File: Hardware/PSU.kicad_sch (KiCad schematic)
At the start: 0 parts

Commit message: included psu on pcb
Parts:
- added C? (x7): 10u, symbol Device:C_Polarized_Small
- added C?: 10n, symbol Device:C_Small
- added C?: 100n, symbol Device:C_Small
- added F?: BELFUSE 430021 2,5A, symbol Device:Fuse_Small
- added L?: BLM21PG 221, symbol Device:L_Ferrite_Small
- added Q?: FDN 337N, symbol Device:Q_NMOS_GSD
- added U? (x3): AP1117-33, Package_TO_SOT_SMD:SOT-223-3_TabPin2, symbol Regulator_Linear:AP1117-33
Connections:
- new net: C?.1, C?.1, C?.1, C?.1, F?.2, L?.1, U?.3 (VI), U?.3 (VI), U?.3 (VI)
- new net: F?.1, Q?.2 (S)
- new net 3V3_0: C?.1, U?.2 (VO)
- new net 3V3_1: C?.1, U?.2 (VO)
- new net 3V3_2: C?.1, U?.2 (VO)
- new net 5V: Q?.3 (D)
- new net GND: C?.2, C?.2, C?.2, C?.2, C?.2, C?.2, C?.2, C?.2, C?.2, Q?.1 (G), U?.1 (GND), U?.1 (GND), U?.1 (GND)
- new net PWR: C?.1, C?.1, L?.2
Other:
- note added: "TODO: 1. LiPo Batterie integration 2. Step Up"

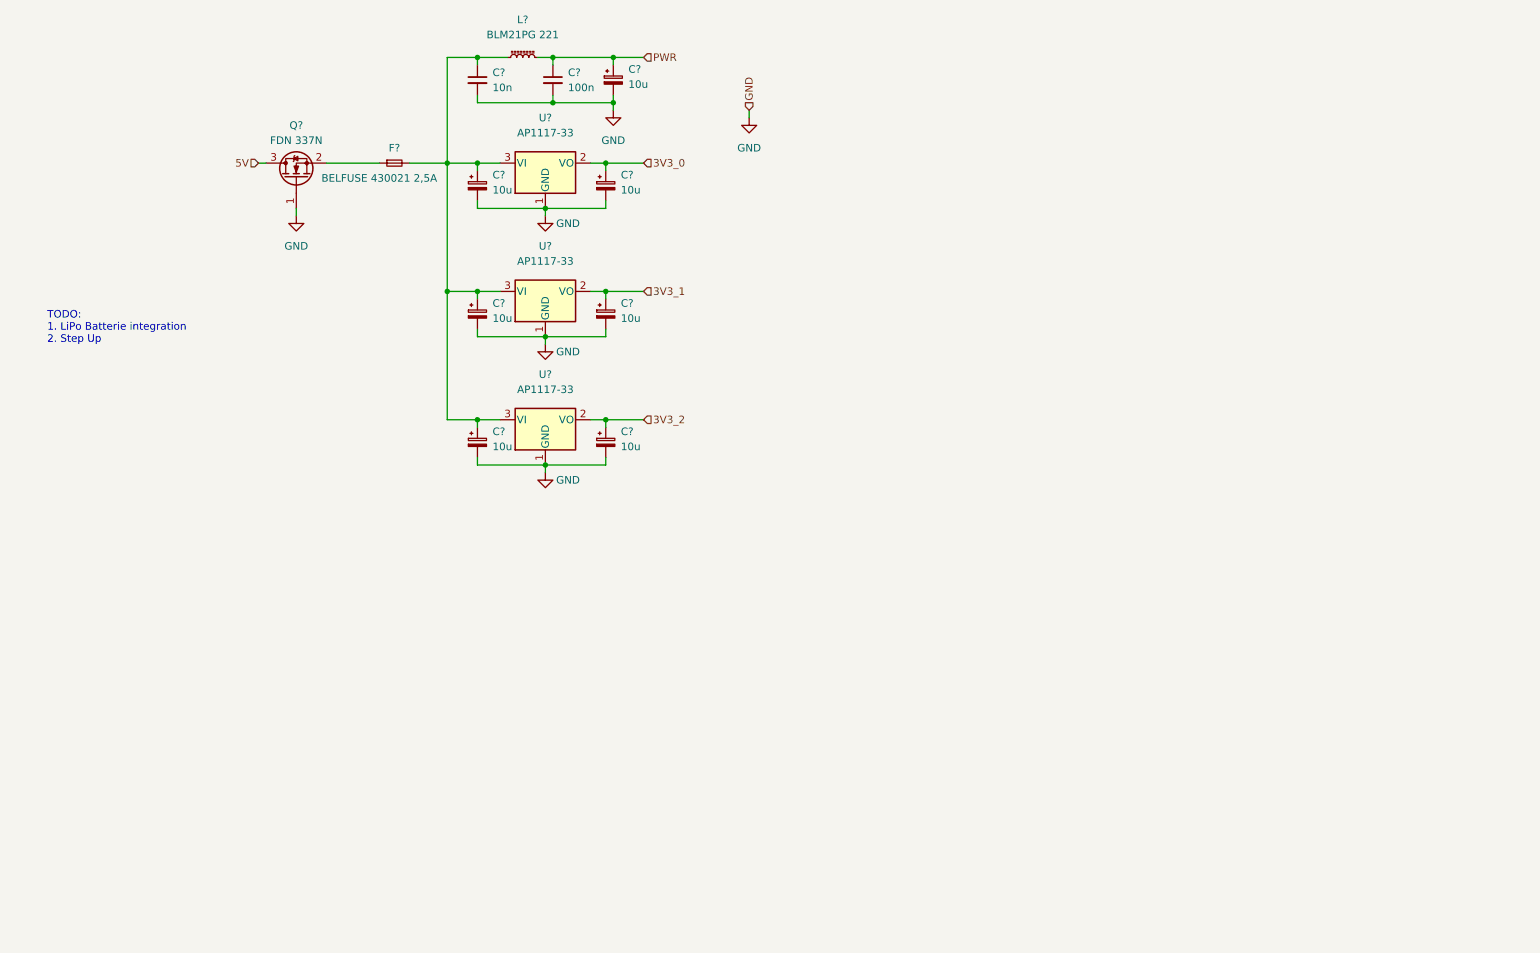
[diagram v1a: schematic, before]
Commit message: added boost converter and shared power
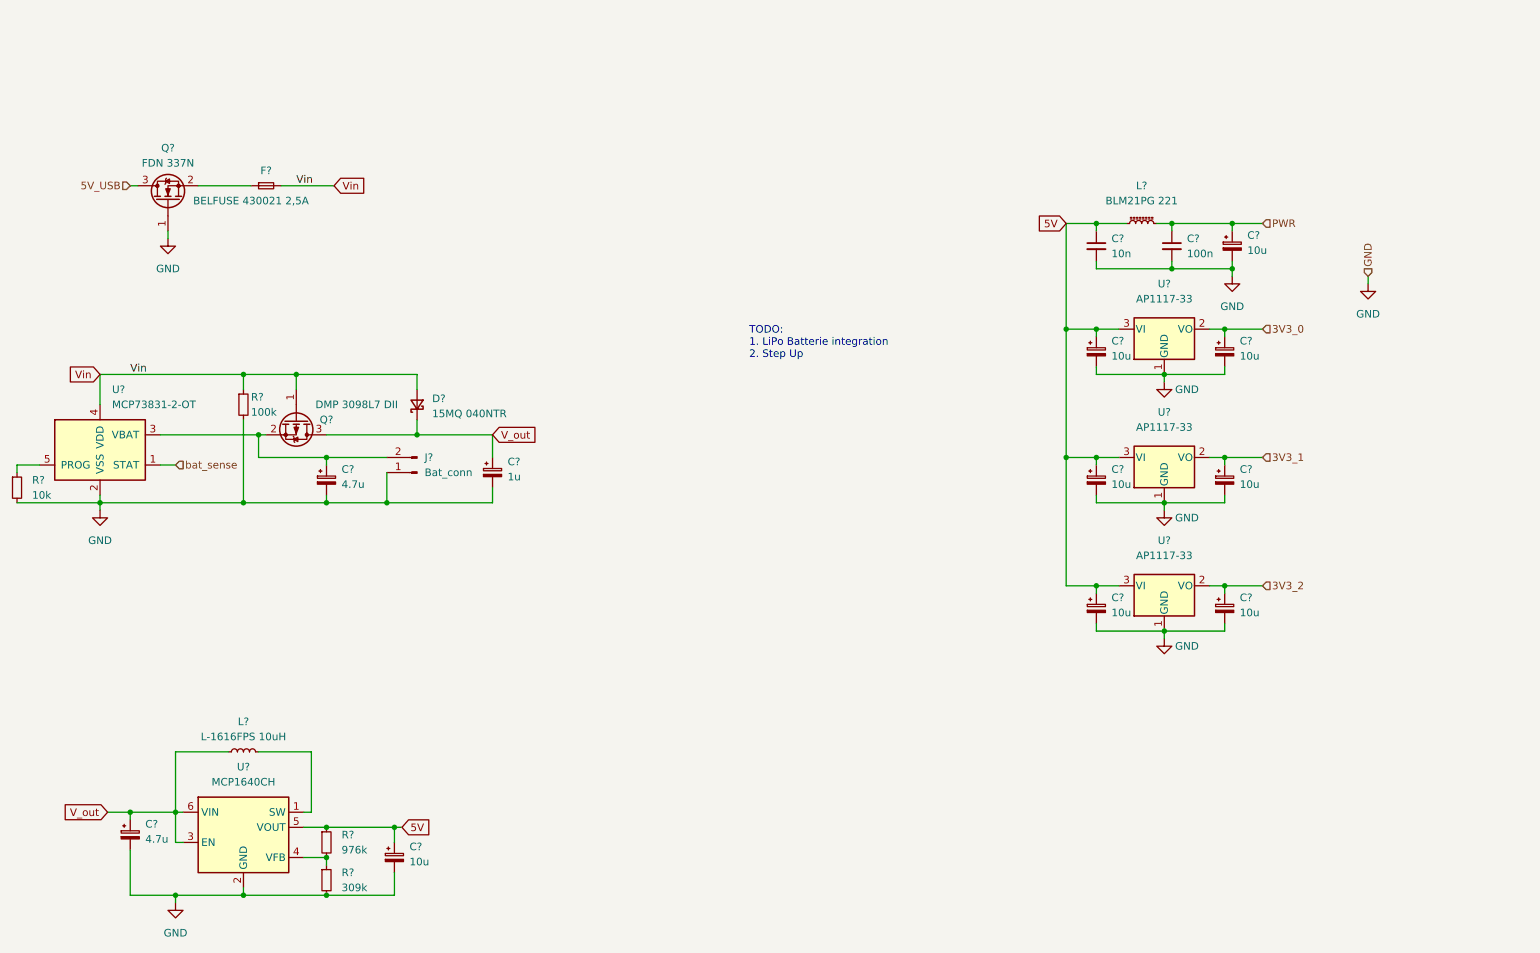
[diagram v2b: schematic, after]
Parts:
- added C?: 1u, symbol Device:C_Polarized_Small
- added C?: 10u, symbol Device:C_Polarized_Small
- added C? (x2): 4.7u, symbol Device:C_Polarized_Small
- added D?: 15MQ 040NTR, symbol Device:D_Schottky_Small
- added J?: Bat_conn, symbol Connector:Conn_01x02_Male
- added L?: L-1616FPS 10uH, symbol Device:L_Small
- added Q?: DMP 3098L7 DII, symbol Device:Q_PMOS_GSD
- added R?: 10k, symbol Device:R_Small
- added R?: 100k, symbol Device:R_Small
- added R?: 976k, symbol Device:R_Small
- added R?: 309k, symbol Device:R_Small
- added U?: MCP1640CH, Package_TO_SOT_SMD:SOT-23-6, symbol Regulator_Switching:MCP1640CH
- added U?: MCP73831-2-OT, Package_TO_SOT_SMD:SOT-23-5, symbol Battery_Management:MCP73831-2-OT
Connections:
- net 5V: now also C?.1, C?.1, C?.1, C?.1, L?.1, U?.3 (VI), U?.3 (VI), U?.3 (VI), C?.1, R?.1, U?.5 (VOUT); no longer Q?.3 (D)
- net GND: now also C?.2, C?.2, C?.2, C?.2, J?.1 (Pin_1), R?.2, R?.2, R?.2, U?.2 (GND), U?.2 (VSS)
- new net: R?.1, U?.5 (PROG)
- new net: L?.2, U?.1 (SW)
- new net: R?.1, R?.2, U?.4 (VFB)
- new net: C?.1, J?.2 (Pin_2), Q?.2 (S), U?.3 (VBAT)
- new net 5V_USB: Q?.3 (D)
- new net V_out: C?.1, C?.1, D?.1 (K), L?.1, Q?.3 (D), U?.3 (EN), U?.6 (VIN)
- new net Vin: D?.2 (A), F?.2, Q?.1 (G), R?.1, U?.4 (VDD)
- new net bat_sense: U?.1 (STAT)
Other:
- moved on the sheet: C?, F?, L?, Q?, U?

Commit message: fixes for hierarchical sheets
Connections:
- net V_out renamed v_out
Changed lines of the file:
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@@
     (stroke (width 0) (type default) (color 0 0 0 0))
   )
-  (wire (pts (xy 93.98 154.94) (xy 95.25 154.94))
+  (wire (pts (xy 93.98 154.94) (xy 99.06 154.94))
     (stroke (width 0) (type default) (color 0 0 0 0))
   )
@@
     (stroke (width 0) (type default) (color 0 0 0 0))
   )
-  (wire (pts (xy 257.81 62.23) (xy 257.81 63.5))
-    (stroke (width 0) (type default) (color 0 0 0 0))
-  )
   (wire (pts (xy 97.79 78.74) (xy 97.79 81.28))
     (stroke (width 0) (type default) (color 0 0 0 0))
@@
     (stroke (width 0) (type default) (color 0 0 0 0))
   )
-  (wire (pts (xy 45.72 152.4) (xy 49.53 152.4))
+  (wire (pts (xy 43.18 152.4) (xy 49.53 152.4))
     (stroke (width 0) (type default) (color 0 0 0 0))
   )
@@
     (effects (font (size 1.27 1.27)) (justify left bottom))
   )
-  (label "Vin" (at 77.47 46.99 0)
+  (label "5V" (at 99.06 154.94 180)
+    (effects (font (size 1.27 1.27)) (justify right bottom))
+  )
+  (label "v_out" (at 43.18 152.4 0)
     (effects (font (size 1.27 1.27)) (justify left bottom))
   )
-  (label "Vin" (at 49.53 78.74 0)
+  (label "v_out" (at 105.41 88.9 0)
     (effects (font (size 1.27 1.27)) (justify left bottom))
   )
-  (global_label "V_out" (shape input) (at 110.49 88.9 0) (fields_autoplaced)
-    (effects (font (size 1.27 1.27)) (justify left))
-    (property "Intersheet References" "${INTERSHEET_REFS}" (id 0) (at 117.9831 88.8206 0)
-      (effects (font (size 1.27 1.27)) (justify left) hide)
-    )
-  )
-  (global_label "5V" (shape input) (at 207.01 53.34 180) (fields_autoplaced)
-    (effects (font (size 1.27 1.27)) (justify right))
-    (property "Intersheet References" "${INTERSHEET_REFS}" (id 0) (at 202.2988 53.2606 0)
-      (effects (font (size 1.27 1.27)) (justify right) hide)
-    )
-  )
-  (global_label "Vin" (shape input) (at 83.82 46.99 0) (fields_autoplaced)
-    (effects (font (size 1.27 1.27)) (justify left))
-    (property "Intersheet References" "${INTERSHEET_REFS}" (id 0) (at 89.0755 46.9106 0)
-      (effects (font (size 1.27 1.27)) (justify left) hide)
-    )
-  )
-  (global_label "Vin" (shape input) (at 44.45 78.74 180) (fields_autoplaced)
-    (effects (font (size 1.27 1.27)) (justify right))
-    (property "Intersheet References" "${INTERSHEET_REFS}" (id 0) (at 39.1945 78.8194 0)
-      (effects (font (size 1.27 1.27)) (justify right) hide)
-    )
-  )
-  (global_label "V_out" (shape input) (at 45.72 152.4 180) (fields_autoplaced)
-    (effects (font (size 1.27 1.27)) (justify right))
-    (property "Intersheet References" "${INTERSHEET_REFS}" (id 0) (at 38.2269 152.4794 0)
-      (effects (font (size 1.27 1.27)) (justify right) hide)
-    )
-  )
-  (global_label "5V" (shape input) (at 95.25 154.94 0) (fields_autoplaced)
-    (effects (font (size 1.27 1.27)) (justify left))
-    (property "Intersheet References" "${INTERSHEET_REFS}" (id 0) (at 99.9612 155.0194 0)
-      (effects (font (size 1.27 1.27)) (justify left) hide)
-    )
+  (label "Vin" (at 83.82 46.99 180)
+    (effects (font (size 1.27 1.27)) (justify right bottom))
+  )
+  (label "Vin" (at 44.45 78.74 0)
+    (effects (font (size 1.27 1.27)) (justify left bottom))
+  )
+  (label "5V" (at 207.01 53.34 0)
+    (effects (font (size 1.27 1.27)) (justify left bottom))
   )
   (hierarchical_label "3V3_0" (shape input) (at 240.03 71.12 0)
@@
   )
   (hierarchical_label "bat_sense" (shape input) (at 57.15 93.98 0)
-    (effects (font (size 1.27 1.27)) (justify left))
-  )
-  (hierarchical_label "GND" (shape input) (at 257.81 62.23 90)
     (effects (font (size 1.27 1.27)) (justify left))
   )
@@
     (pin "2")
   )
-  (symbol (lib_id "power:GND") (at 257.81 63.5 0) (unit 1)
-    (in_bom yes) (on_board yes) (fields_autoplaced)
-    (property "Reference" "#PWR?" (id 0) (at 257.81 69.85 0)
-      (effects (font (size 1.27 1.27)) hide)
-    )
-    (property "Value" "GND" (id 1) (at 257.81 68.58 0))
-    (property "Footprint" "" (id 2) (at 257.81 63.5 0)
-      (effects (font (size 1.27 1.27)) hide)
-    )
-    (property "Datasheet" "" (id 3) (at 257.81 63.5 0)
-      (effects (font (size 1.27 1.27)) hide)
-    )
-    (pin "1")
-  )
 )

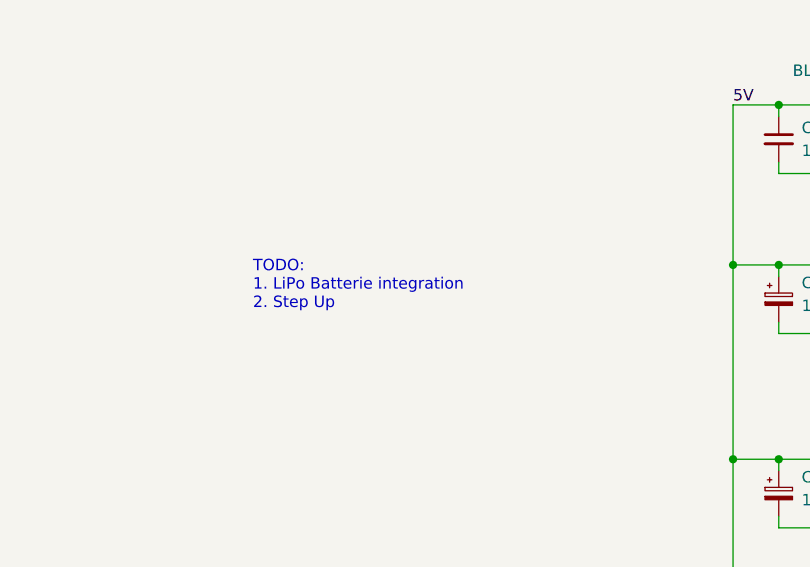
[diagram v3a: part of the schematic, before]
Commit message: added hierrarchial labels
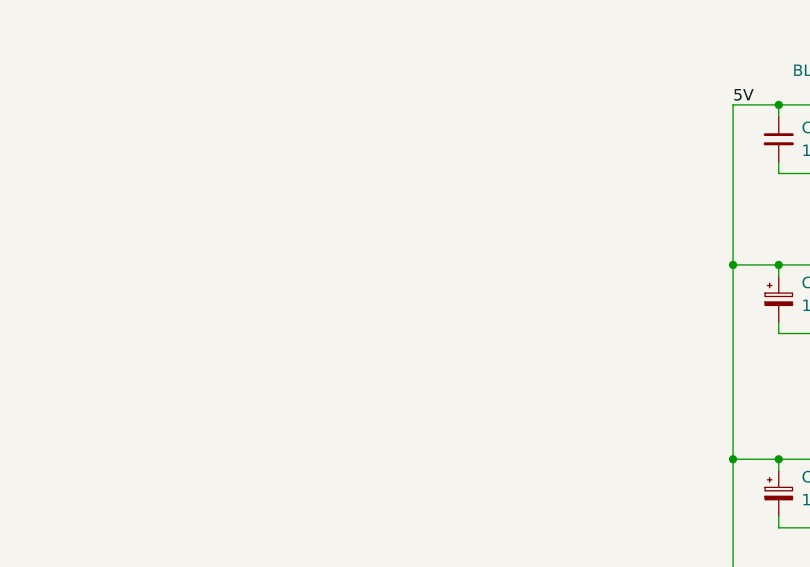
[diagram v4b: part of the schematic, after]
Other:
- note removed: "TODO: 1. LiPo Batterie integration 2. Step Up"
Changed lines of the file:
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@@
     (stroke (width 0) (type default) (color 0 0 0 0))
-  )
-  (text "TODO:\n1. LiPo Batterie integration\n2. Step Up \n" (at 153.67 76.2 0)
-    (effects (font (size 1.27 1.27)) (justify left bottom))
   )
   (label "5V" (at 99.06 154.94 180)

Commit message: cleaned up busses
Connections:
- net v_out: now also Q?.2 (S); no longer Q?.3 (D)
- net at C?.1, J?.2 (Pin_2), U?.3 (VBAT): now also Q?.3 (D); no longer Q?.2 (S)
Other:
- note added: "Place the 3V3 PSUs near to the components that need it (SD card, display, uC ect)"
- note added: "TODO: Bypass boost converter wehn charging"
- moved on the sheet: C?, J?, Q?
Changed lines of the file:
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@@
   (junction (at 77.47 78.74) (diameter 0) (color 0 0 0 0)
   )
+  (junction (at 71.12 92.71) (diameter 0) (color 0 0 0 0)
+  )
   (junction (at 233.68 114.3) (diameter 0) (color 0 0 0 0)
   )
@@
   (junction (at 224.79 60.96) (diameter 0) (color 0 0 0 0)
   )
+  (junction (at 83.82 100.33) (diameter 0) (color 0 0 0 0)
+  )
   (junction (at 212.09 92.71) (diameter 0) (color 0 0 0 0)
   )
-  (junction (at 92.71 100.33) (diameter 0) (color 0 0 0 0)
-  )
   (junction (at 68.58 100.33) (diameter 0) (color 0 0 0 0)
   )
@@
   (junction (at 223.52 78.74) (diameter 0) (color 0 0 0 0)
   )
-  (junction (at 82.55 92.71) (diameter 0) (color 0 0 0 0)
-  )
   (junction (at 223.52 121.92) (diameter 0) (color 0 0 0 0)
   )
@@
   (junction (at 234.95 53.34) (diameter 0) (color 0 0 0 0)
   )
+  (junction (at 71.12 100.33) (diameter 0) (color 0 0 0 0)
+  )
   (junction (at 82.55 166.37) (diameter 0) (color 0 0 0 0)
   )
@@
   (junction (at 57.15 152.4) (diameter 0) (color 0 0 0 0)
   )
-  (junction (at 82.55 100.33) (diameter 0) (color 0 0 0 0)
-  )
   (wire (pts (xy 212.09 71.12) (xy 212.09 72.39))
     (stroke (width 0) (type default) (color 0 0 0 0))
@@
     (stroke (width 0) (type default) (color 0 0 0 0))
   )
+  (wire (pts (xy 83.82 100.33) (xy 110.49 100.33))
+    (stroke (width 0) (type default) (color 0 0 0 0))
+  )
   (wire (pts (xy 93.98 154.94) (xy 93.98 157.48))
     (stroke (width 0) (type default) (color 0 0 0 0))
@@
     (stroke (width 0) (type default) (color 0 0 0 0))
   )
-  (wire (pts (xy 82.55 100.33) (xy 92.71 100.33))
+  (wire (pts (xy 71.12 100.33) (xy 83.82 100.33))
     (stroke (width 0) (type default) (color 0 0 0 0))
   )
@@
     (stroke (width 0) (type default) (color 0 0 0 0))
   )
-  (wire (pts (xy 71.12 92.71) (xy 82.55 92.71))
-    (stroke (width 0) (type default) (color 0 0 0 0))
-  )
   (wire (pts (xy 223.52 78.74) (xy 223.52 80.01))
     (stroke (width 0) (type default) (color 0 0 0 0))
@@
     (stroke (width 0) (type default) (color 0 0 0 0))
   )
-  (wire (pts (xy 92.71 100.33) (xy 92.71 95.25))
-    (stroke (width 0) (type default) (color 0 0 0 0))
-  )
-  (wire (pts (xy 110.49 100.33) (xy 92.71 100.33))
+  (wire (pts (xy 83.82 100.33) (xy 83.82 95.25))
     (stroke (width 0) (type default) (color 0 0 0 0))
   )
@@
     (stroke (width 0) (type default) (color 0 0 0 0))
   )
-  (wire (pts (xy 82.55 92.71) (xy 92.71 92.71))
+  (wire (pts (xy 71.12 92.71) (xy 83.82 92.71))
     (stroke (width 0) (type default) (color 0 0 0 0))
   )
@@
     (stroke (width 0) (type default) (color 0 0 0 0))
   )
-  (wire (pts (xy 82.55 92.71) (xy 82.55 93.98))
+  (wire (pts (xy 71.12 92.71) (xy 71.12 93.98))
     (stroke (width 0) (type default) (color 0 0 0 0))
   )
@@
     (stroke (width 0) (type default) (color 0 0 0 0))
   )
-  (wire (pts (xy 82.55 99.06) (xy 82.55 100.33))
-    (stroke (width 0) (type default) (color 0 0 0 0))
-  )
-  (wire (pts (xy 68.58 100.33) (xy 82.55 100.33))
+  (wire (pts (xy 71.12 99.06) (xy 71.12 100.33))
+    (stroke (width 0) (type default) (color 0 0 0 0))
+  )
+  (wire (pts (xy 68.58 100.33) (xy 71.12 100.33))
     (stroke (width 0) (type default) (color 0 0 0 0))
   )
@@
   (wire (pts (xy 80.01 142.24) (xy 80.01 152.4))
     (stroke (width 0) (type default) (color 0 0 0 0))
+  )
+  (text "TODO: Bypass boost converter wehn charging" (at 46.99 133.35 0)
+    (effects (font (size 1.27 1.27)) (justify left bottom))
+  )
+  (text "Place the 3V3 PSUs near to the components that need it (SD card, display, uC ect)"
+    (at 186.69 41.91 0)
+    (effects (font (size 1.27 1.27)) (justify left bottom))
   )
   (label "5V" (at 99.06 154.94 180)
@@
     (pin "5")
   )
-  (symbol (lib_id "Connector:Conn_01x02_Male") (at 97.79 95.25 180) (unit 1)
-    (in_bom yes) (on_board yes) (fields_autoplaced)
-    (property "Reference" "J?" (id 0) (at 99.06 92.7099 0)
+  (symbol (lib_id "Connector:Conn_01x02_Male") (at 88.9 95.25 180) (unit 1)
+    (in_bom yes) (on_board yes) (fields_autoplaced)
+    (property "Reference" "J?" (id 0) (at 90.17 92.7099 0)
       (effects (font (size 1.27 1.27)) (justify right))
     )
-    (property "Value" "Bat_conn" (id 1) (at 99.06 95.2499 0)
+    (property "Value" "Bat_conn" (id 1) (at 90.17 95.2499 0)
       (effects (font (size 1.27 1.27)) (justify right))
     )
-    (property "Footprint" "" (id 2) (at 97.79 95.25 0)
-      (effects (font (size 1.27 1.27)) hide)
-    )
-    (property "Datasheet" "~" (id 3) (at 97.79 95.25 0)
+    (property "Footprint" "" (id 2) (at 88.9 95.25 0)
+      (effects (font (size 1.27 1.27)) hide)
+    )
+    (property "Datasheet" "~" (id 3) (at 88.9 95.25 0)
       (effects (font (size 1.27 1.27)) hide)
     )
@@
     (pin "3")
   )
-  (symbol (lib_id "Device:C_Polarized_Small") (at 82.55 96.52 0) (unit 1)
-    (in_bom yes) (on_board yes) (fields_autoplaced)
-    (property "Reference" "C?" (id 0) (at 85.09 94.7038 0)
-      (effects (font (size 1.27 1.27)) (justify left))
-    )
-    (property "Value" "4.7u" (id 1) (at 85.09 97.2438 0)
-      (effects (font (size 1.27 1.27)) (justify left))
-    )
-    (property "Footprint" "" (id 2) (at 82.55 96.52 0)
-      (effects (font (size 1.27 1.27)) hide)
-    )
-    (property "Datasheet" "~" (id 3) (at 82.55 96.52 0)
+  (symbol (lib_id "Device:C_Polarized_Small") (at 71.12 96.52 0) (unit 1)
+    (in_bom yes) (on_board yes) (fields_autoplaced)
+    (property "Reference" "C?" (id 0) (at 73.66 94.7038 0)
+      (effects (font (size 1.27 1.27)) (justify left))
+    )
+    (property "Value" "4.7u" (id 1) (at 73.66 97.2438 0)
+      (effects (font (size 1.27 1.27)) (justify left))
+    )
+    (property "Footprint" "" (id 2) (at 71.12 96.52 0)
+      (effects (font (size 1.27 1.27)) hide)
+    )
+    (property "Datasheet" "~" (id 3) (at 71.12 96.52 0)
       (effects (font (size 1.27 1.27)) hide)
     )
@@
     (in_bom yes) (on_board yes)
     (property "Reference" "F?" (id 0) (at 72.39 44.45 0))
-    (property "Value" "BELFUSE 430021 2,5A" (id 1) (at 69.85 49.53 0))
+    (property "Value" "BELFUSE 430021 2,5A" (id 1) (at 76.2 49.53 0))
     (property "Footprint" "" (id 2) (at 72.39 46.99 0)
       (effects (font (size 1.27 1.27)) hide)
@@
     (pin "2")
   )
-  (symbol (lib_id "Device:Q_PMOS_GSD") (at 77.47 86.36 270) (unit 1)
+  (symbol (lib_id "Device:Q_PMOS_GSD") (at 77.47 86.36 90) (mirror x) (unit 1)
     (in_bom yes) (on_board yes)
-    (property "Reference" "Q?" (id 0) (at 82.55 86.36 90))
-    (property "Value" "DMP 3098L7 DII" (id 1) (at 87.63 83.82 90))
-    (property "Footprint" "" (id 2) (at 80.01 91.44 0)
-      (effects (font (size 1.27 1.27)) hide)
-    )
+    (property "Reference" "Q?" (id 0) (at 81.28 85.09 90))
+    (property "Value" "DMP 3098L7 DII" (id 1) (at 85.6718 80.8692 90))
+    (property "Footprint" "" (id 2) (at 74.93 91.44 0)
+      (effects (font (size 1.27 1.27)) hide)
+    )
